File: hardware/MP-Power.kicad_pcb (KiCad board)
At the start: 2 copper layers, 17 x 14.8 mm, 12 parts, among them U1 MP1584EN

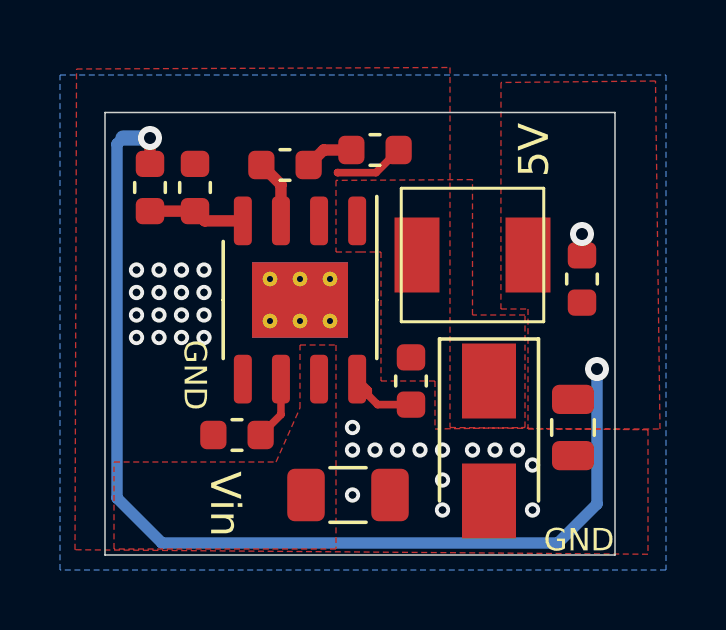
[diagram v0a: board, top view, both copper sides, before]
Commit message: Update MP-Power design with a 3.2A inductor.
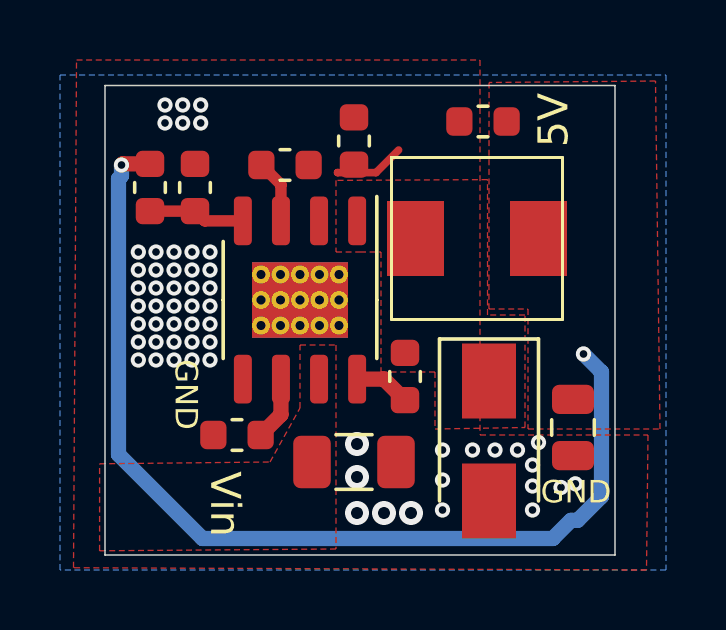
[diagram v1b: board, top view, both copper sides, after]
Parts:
- L1: footprint PrntrBoardV2:MWSA0402S -> PrntrBoardV2:MWSA0503
- moved C5 6.20 mm to (120.1, 72.5), turned to 180 degrees
- moved C1 1.12 mm to (115.8, 83.9)
- moved R2 0.76 mm to (115.8, 73.2), turned to 90 degrees
- moved L1 0.57 mm to (119.9, 76.5)
- moved C2 0.25 mm to (117.5, 81.0)
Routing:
- net /5V: track 35.5 -> 33.5 mm
- net Net-(C3-Pad2): track 1.63 -> 0.00 mm
- net GND: track 3.06 -> 2.35 mm, vias 31 -> 58
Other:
- board size 17 x 14.8 mm -> 17 x 15.7 mm

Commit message: Route one missed trace.
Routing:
- net GND: track 2.35 -> 0.00 mm
- net Net-(C3-Pad2): track 0.00 -> 1.52 mm

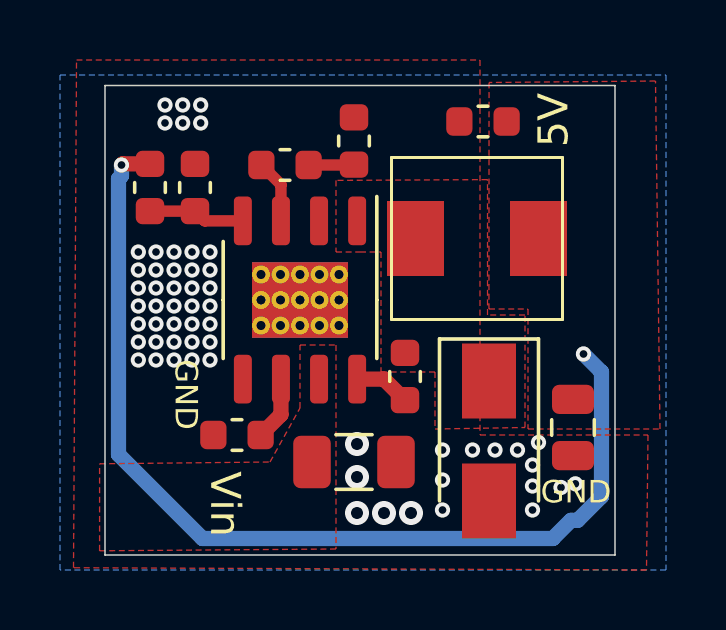
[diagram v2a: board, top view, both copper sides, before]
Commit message: Update libraries to match the latest Windows release. Fix DRC issues.
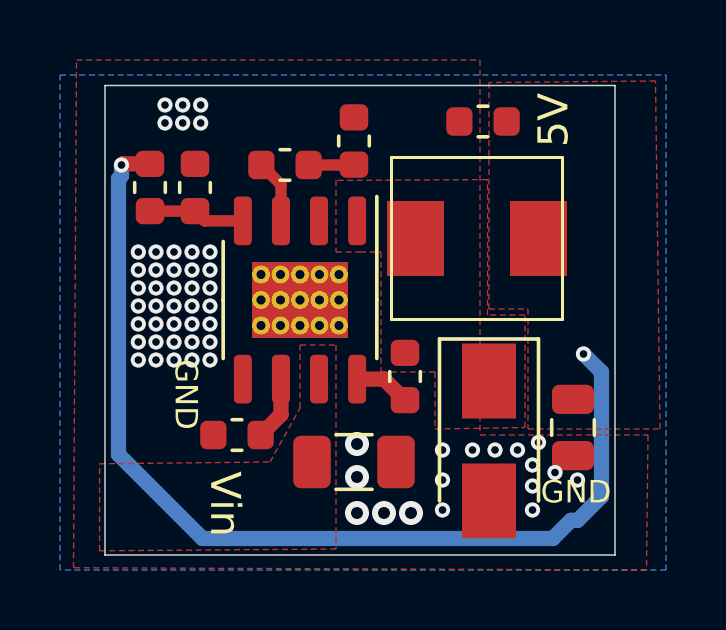
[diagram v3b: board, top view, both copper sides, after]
